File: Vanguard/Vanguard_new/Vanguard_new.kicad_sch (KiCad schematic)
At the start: 72 parts, among them J1 USB_C, J2 Conn_02x03_Pin, J3 Micro_SD_Card_Det1, J4 STARBOARD_SERVO, J5 PORTSIDE_SERVO, J6 LIPO_in, Q1 BSS138, Q2 BSS138, Q3 BSS138, U1 ATSAMD11D14A-M, U2 ATmega4809-A, U3 AT25DF641A-SH-T, U4 AP2112K-3.3, U5 MPM3610AGQV-P, U6 BNO086, U7 TXB0104D, U8 TPS61092, Y1 32.768kHz

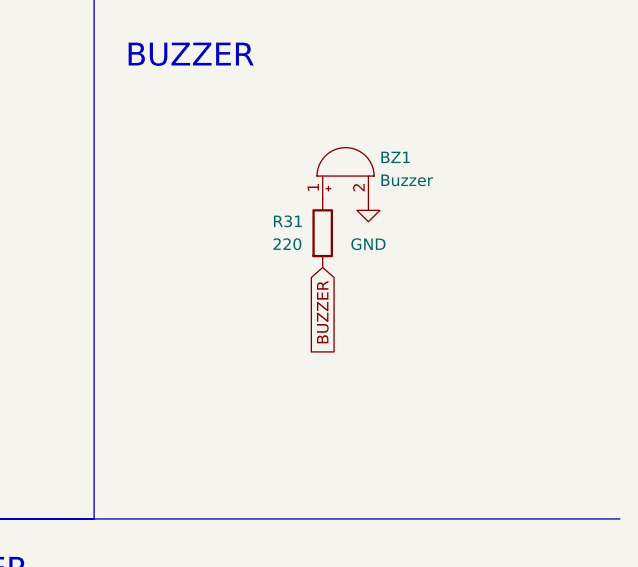
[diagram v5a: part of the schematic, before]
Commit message: buzzer redone
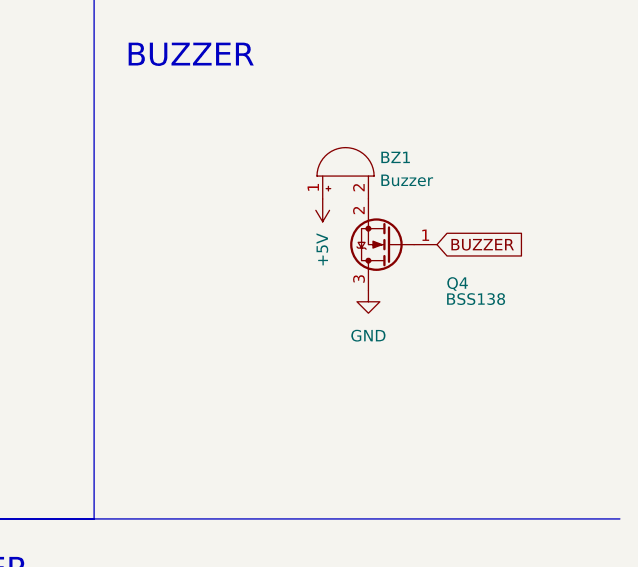
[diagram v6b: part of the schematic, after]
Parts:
- removed R31: 220, symbol Device:R
- added Q4: BSS138, Package_TO_SOT_SMD:SOT-23, symbol Transistor_FET:BSS138
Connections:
- net +5V: now also BZ1.1 (+)
- net BUZZER: now also Q4.1 (G)
- net GND: now also Q4.3 (D); no longer BZ1.2 (-)
- new net: BZ1.2 (-), Q4.2 (S)
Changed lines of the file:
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@@
 	(global_label "BUZZER"
 		(shape input)
-		(at 386.08 111.76 270)
+		(at 398.78 109.22 0)
 		(fields_autoplaced yes)
 		(effects
@@
 				(size 1.27 1.27)
 			)
-			(justify right)
+			(justify left)
 		)
 		(property "Intersheetrefs" "${INTERSHEET_REFS}"
-			(at 386.08 122.1837 90)
+			(at 409.2037 109.22 0)
 			(effects
 				(font
 					(size 1.27 1.27)
 				)
-				(justify right)
+				(justify left)
 				(hide yes)
 			)
@@
 	(symbol
 		(lib_id "power:GND")
-		(at 391.16 104.14 0)
+		(at 391.16 114.3 0)
 		(unit 1)
 		(exclude_from_sim no)
@@
 		(fields_autoplaced yes)
 		(property "Reference" "#PWR070"
-			(at 391.16 110.49 0)
+			(at 391.16 120.65 0)
 			(effects
 				(font
@@
 		)
 		(property "Value" "GND"
-			(at 391.16 109.22 0)
+			(at 391.16 119.38 0)
 			(effects
 				(font
@@
 		)
 		(property "Footprint" ""
-			(at 391.16 104.14 0)
+			(at 391.16 114.3 0)
 			(effects
 				(font
@@
 		)
 		(property "Datasheet" ""
-			(at 391.16 104.14 0)
+			(at 391.16 114.3 0)
 			(effects
 				(font
@@
 		)
 		(property "Description" "Power symbol creates a global label with name \"GND\" , ground"
-			(at 391.16 104.14 0)
+			(at 391.16 114.3 0)
 			(effects
 				(font
@@
 	(symbol
 		(lib_id "Device:R")
-		(at 386.08 107.95 0)
-		(unit 1)
-		(exclude_from_sim no)
-		(in_bom yes)
-		(on_board yes)
-		(dnp no)
-		(property "Reference" "R31"
-			(at 380.492 106.68 0)
-			(effects
-				(font
-					(size 1.27 1.27)
-				)
-				(justify left)
-			)
-		)
-		(property "Value" "220"
-			(at 380.492 109.22 0)
-			(effects
-				(font
-					(size 1.27 1.27)
-				)
-				(justify left)
-			)
-		)
-		(property "Footprint" ""
-			(at 384.302 107.95 90)
-			(effects
-				(font
-					(size 1.27 1.27)
-				)
-				(hide yes)
-			)
-		)
-		(property "Datasheet" "~"
-			(at 386.08 107.95 0)
-			(effects
-				(font
-					(size 1.27 1.27)
-				)
-				(hide yes)
-			)
-		)
-		(property "Description" "Resistor"
-			(at 386.08 107.95 0)
-			(effects
-				(font
-					(size 1.27 1.27)
-				)
-				(hide yes)
-			)
-		)
-		(pin "2"
-		)
-		(pin "1"
-		)
-		(instances
-			(project ""
-				(path "/972fbf12-2dcd-4fdf-b1c9-8a2880c46640"
-					(reference "R31")
-					(unit 1)
-				)
-			)
-		)
-	)
-	(symbol
-		(lib_id "Device:R")
 		(at 167.64 48.26 90)
 		(unit 1)
@@
 	)
 	(symbol
+		(lib_id "power:+5V")
+		(at 386.08 104.14 180)
+		(unit 1)
+		(exclude_from_sim no)
+		(in_bom yes)
+		(on_board yes)
+		(dnp no)
+		(fields_autoplaced yes)
+		(property "Reference" "#PWR071"
+			(at 386.08 100.33 0)
+			(effects
+				(font
+					(size 1.27 1.27)
+				)
+				(hide yes)
+			)
+		)
+		(property "Value" "+5V"
+			(at 386.0801 107.95 90)
+			(effects
+				(font
+					(size 1.27 1.27)
+				)
+				(justify left)
+			)
+		)
+		(property "Footprint" ""
+			(at 386.08 104.14 0)
+			(effects
+				(font
+					(size 1.27 1.27)
+				)
+				(hide yes)
+			)
+		)
+		(property "Datasheet" ""
+			(at 386.08 104.14 0)
+			(effects
+				(font
+					(size 1.27 1.27)
+				)
+				(hide yes)
+			)
+		)
+		(property "Description" "Power symbol creates a global label with name \"+5V\""
+			(at 386.08 104.14 0)
+			(effects
+				(font
+					(size 1.27 1.27)
+				)
+				(hide yes)
+			)
+		)
+		(pin "1"
+		)
+		(instances
+			(project "Vanguard_new"
+				(path "/972fbf12-2dcd-4fdf-b1c9-8a2880c46640"
+					(reference "#PWR071")
+					(unit 1)
+				)
+			)
+		)
+	)
+	(symbol
 		(lib_id "BNO086:BNO086")
 		(at 104.14 156.21 0)
@@
 					(unit 1)
 				)
+			)
+		)
+	)
+	(symbol
+		(lib_id "Transistor_FET:BSS138")
+		(at 393.7 109.22 180)
+		(unit 1)
+		(exclude_from_sim no)
+		(in_bom yes)
+		(on_board yes)
+		(dnp no)
+		(property "Reference" "Q4"
+			(at 401.066 113.538 0)
+			(effects
+				(font
+					(size 1.27 1.27)
+				)
+			)
+		)
+		(property "Value" "BSS138"
+			(at 403.098 115.316 0)
+			(effects
+				(font
+					(size 1.27 1.27)
+				)
+			)
+		)
+		(property "Footprint" "Package_TO_SOT_SMD:SOT-23"
+			(at 388.62 107.315 0)
+			(effects
+				(font
+					(size 1.27 1.27)
+					(italic yes)
+				)
+				(justify left)
+				(hide yes)
+			)
+		)
+		(property "Datasheet" "https://www.onsemi.com/pub/Collateral/BSS138-D.PDF"
+			(at 388.62 105.41 0)
+			(effects
+				(font
+					(size 1.27 1.27)
+				)
+				(justify left)
+				(hide yes)
+			)
+		)
+		(property "Description" "50V Vds, 0.22A Id, N-Channel MOSFET, SOT-23"
+			(at 393.7 109.22 0)
+			(effects
+				(font
+					(size 1.27 1.27)
+				)
+				(hide yes)
+			)
+		)
+		(pin "2"
+		)
+		(pin "3"
+		)
+		(pin "1"
+		)
+		(instances
+			(project ""
+				(path "/972fbf12-2dcd-4fdf-b1c9-8a2880c46640"
+					(reference "Q4")
+					(unit 1)
+				)
